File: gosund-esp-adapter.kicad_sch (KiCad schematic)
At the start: 10 parts, among them J1 Connector, J2 Conn_01x04_Male, J3 Conn_01x01_Male, U1 ESP-M2

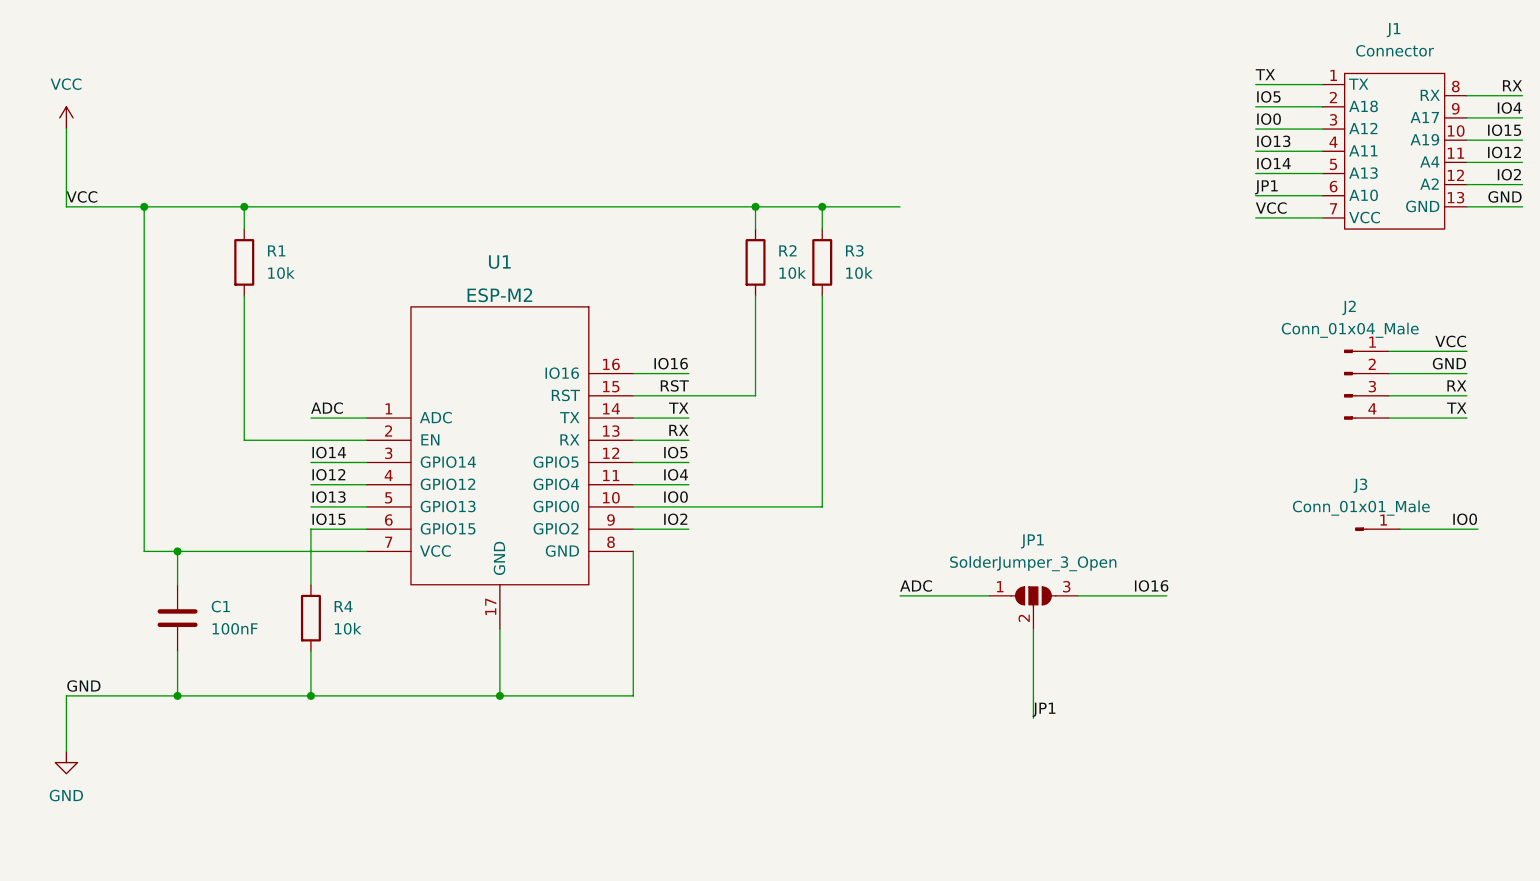
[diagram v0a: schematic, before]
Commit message: modified to match the footprint of an ESP12f module
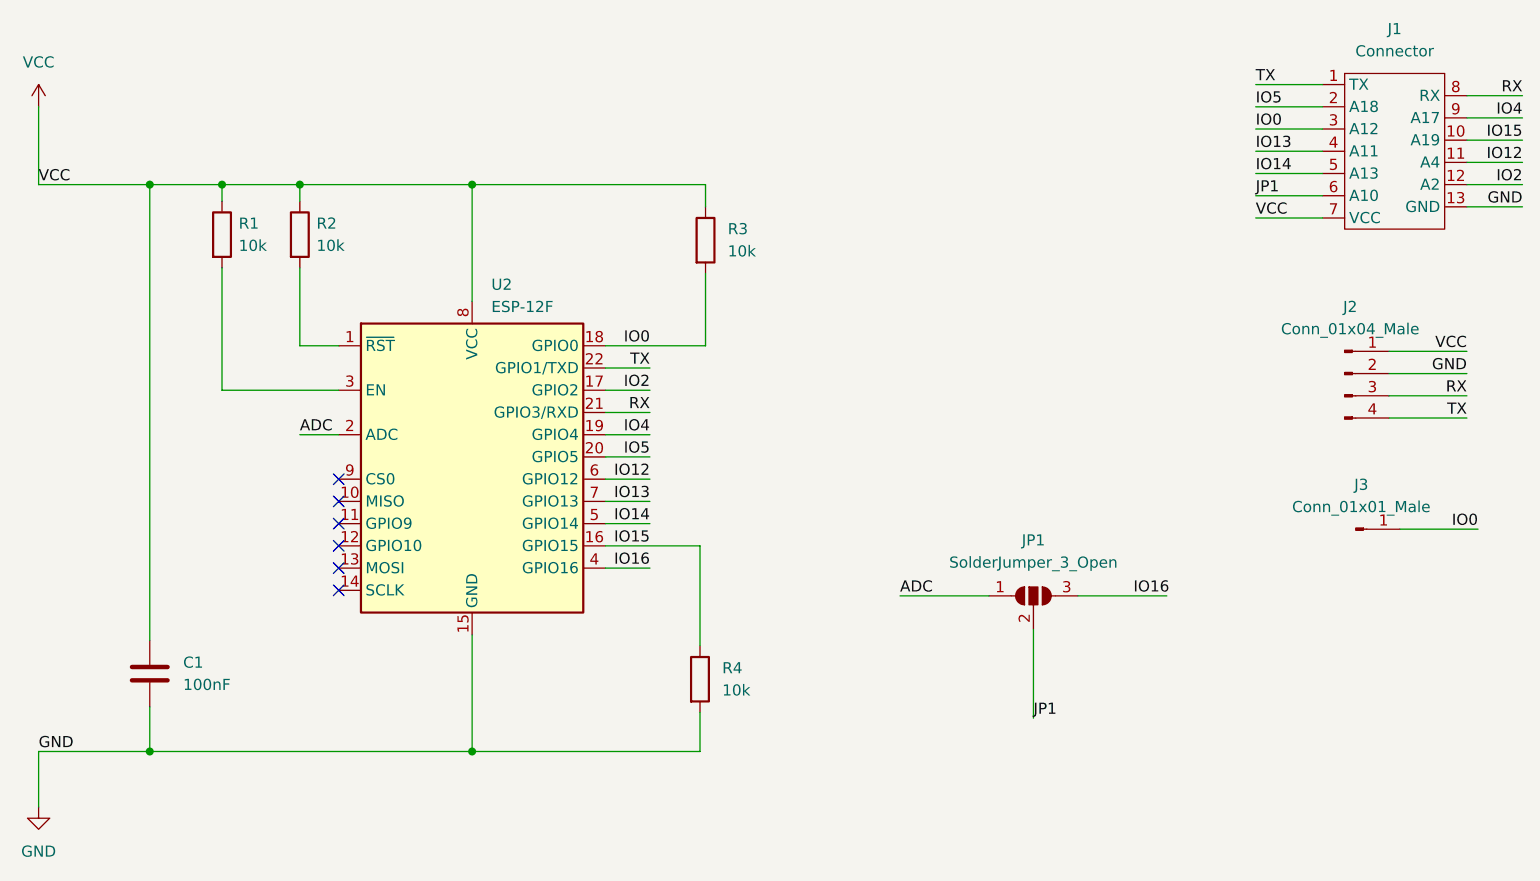
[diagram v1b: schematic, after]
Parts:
- removed U1: ESP-M2, ESP8285:ESP-M2, symbol ESP8285:ESP-M2
- added U2: ESP-12F, RF_Module:ESP-12E, symbol RF_Module:ESP-12F
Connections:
- net ADC: now also U2.2 (ADC)
- net GND: now also U2.15 (GND)
- net IO0: now also U2.18 (GPIO0)
- net IO12: now also U2.6 (GPIO12)
- net IO13: now also U2.7 (GPIO13)
- net IO14: now also U2.5 (GPIO14)
- net IO15: now also U2.16 (GPIO15)
- net IO16: now also U2.4 (GPIO16)
- net IO2: now also U2.17 (GPIO2)
- net IO4: now also U2.19 (GPIO4)
- net IO5: now also U2.20 (GPIO5)
- net RX: now also U2.21 (GPIO3/RXD)
- net TX: now also U2.22 (GPIO1/TXD)
- net VCC: now also U2.8 (VCC)
- net at R1.2: now also U2.3 (EN)
- net RST: no longer names the net of R2.2
- net RST: now also U2.1 (~{RST})
- no-connect marks 0 -> 6
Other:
- company: chrisklinger.de -> ColossalTurtle unip lda
